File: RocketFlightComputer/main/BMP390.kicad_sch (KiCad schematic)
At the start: 3 parts

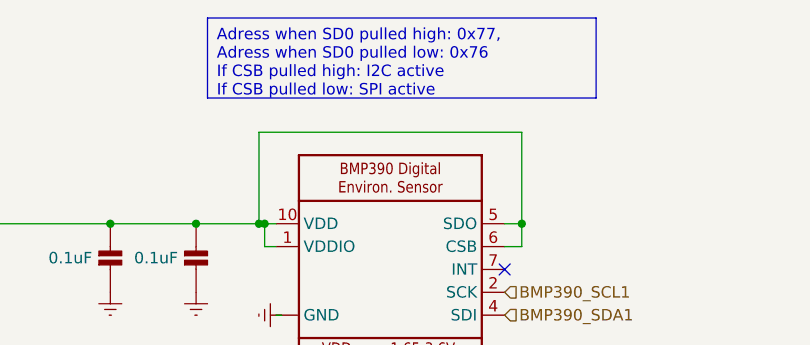
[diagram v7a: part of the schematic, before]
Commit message: Change of winbond flash to other one supported by teensy bootloader since winbond is out of stock
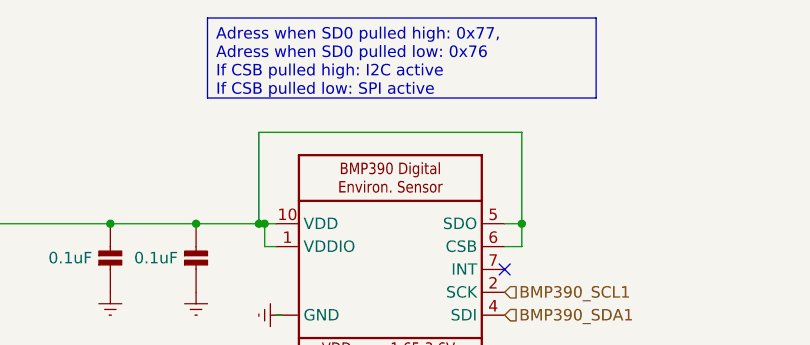
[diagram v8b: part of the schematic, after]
